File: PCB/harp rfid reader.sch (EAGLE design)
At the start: 38 parts, among them IC1 FT232RL, IC2 LP5907MFX-3.3, IC3 ATXMEGAxxxA4U-AU, Q1 BC817-40W, U1 ID-12/20SMD

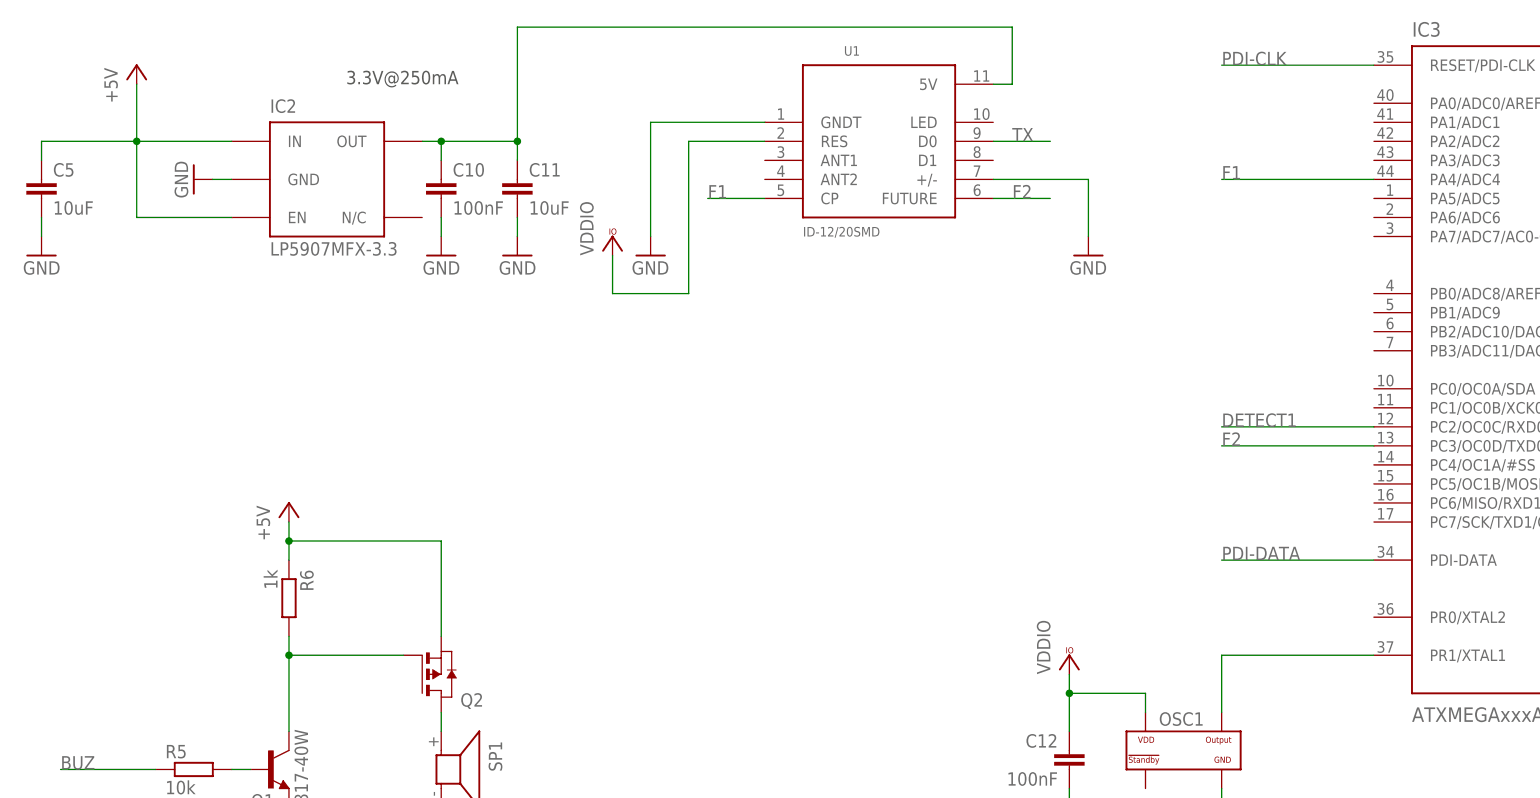
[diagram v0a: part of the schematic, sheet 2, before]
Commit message: Added 3 new capacitors.
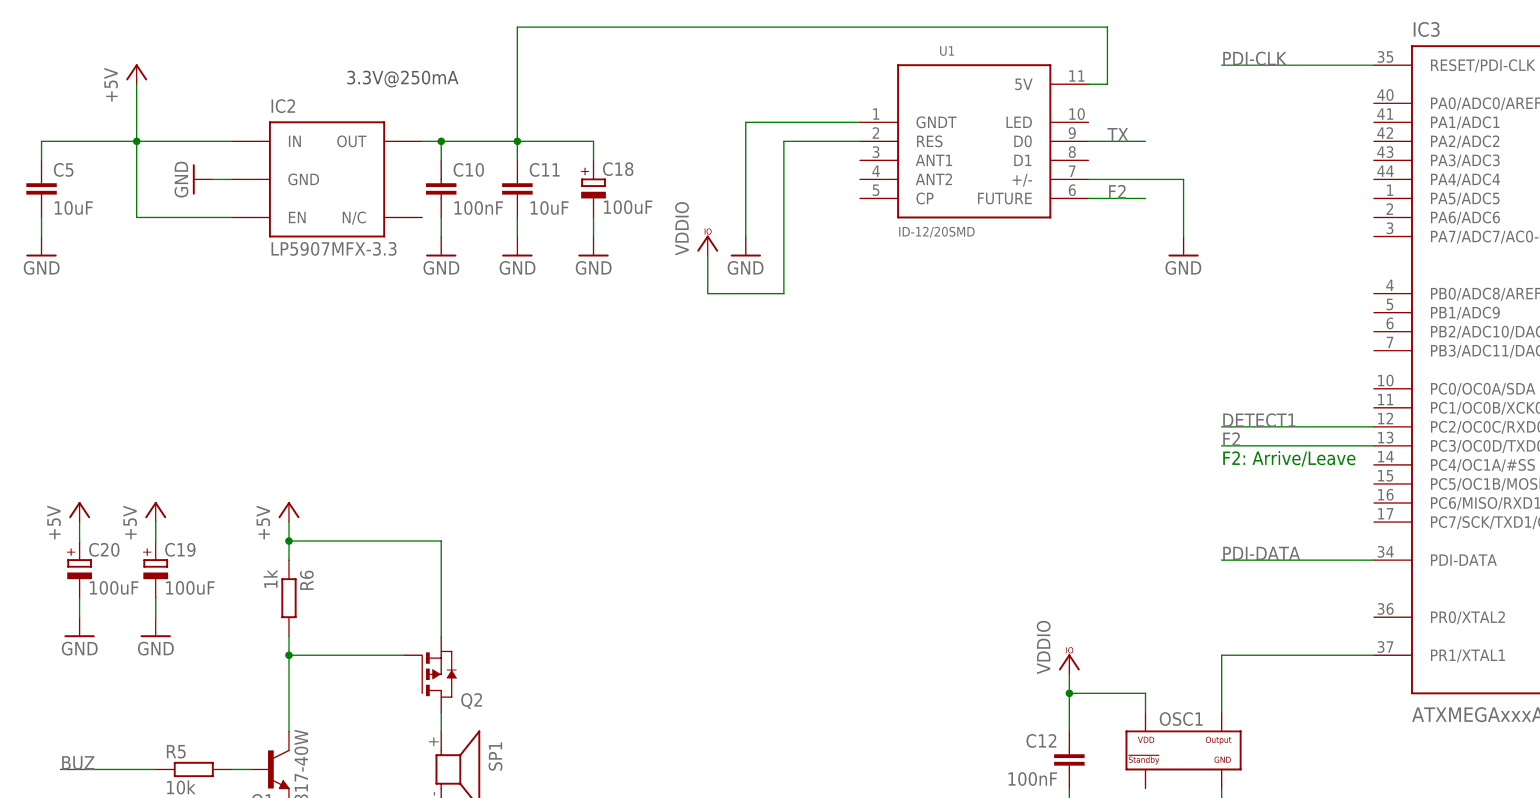
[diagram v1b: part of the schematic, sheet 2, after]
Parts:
- added C18, C19, C20: 100uF, rcl:CPOL-EUCT3216
- C7: value 4.7uF -> 10uF; device rcl:CPOL-EUA/3216-18W -> rcl:C-EUC0603
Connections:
- removed net F1: IC3.PA4/ADC4, U1.CP
- net +5V: now also C19.+, C20.+, C7.1; no longer C7.+
- net GND: now also C18.-, C19.-, C20.-, C7.2; no longer C7.-
- net N$1: now also C18.+
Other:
- note added: "F2: Arrive/Leave"
- note removed: "Case A"
- moved on the sheet: U1

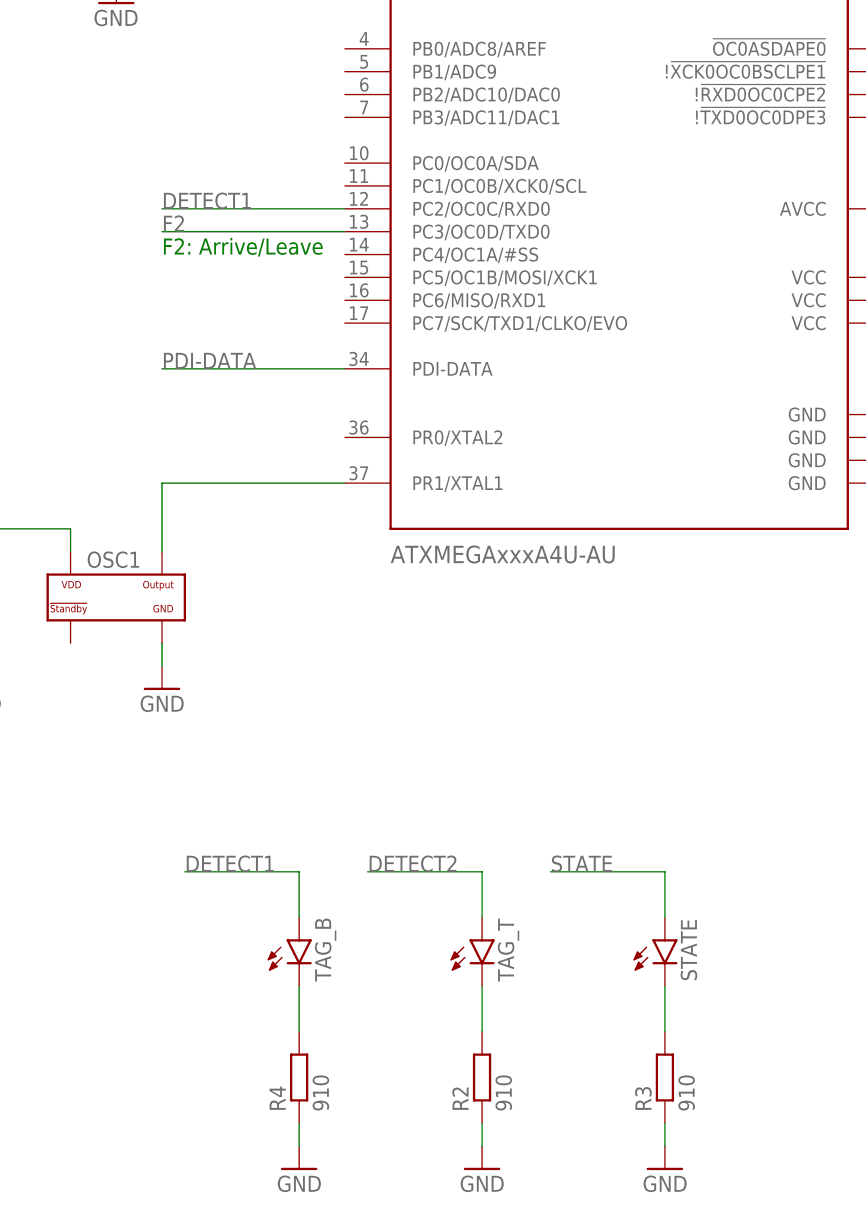
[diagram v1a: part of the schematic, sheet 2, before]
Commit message: Corrected STATE and DETECT lines and increased LED resistors.
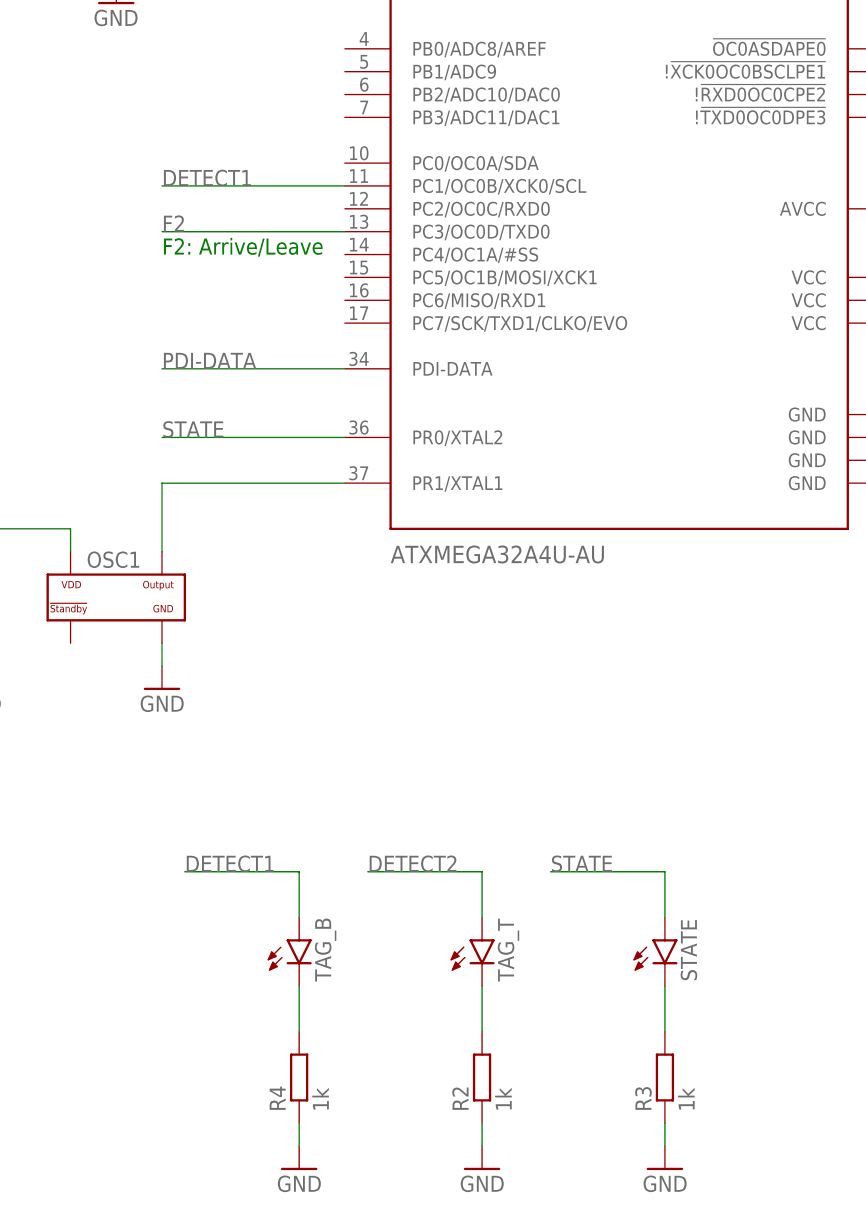
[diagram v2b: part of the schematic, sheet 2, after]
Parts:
- IC3: value ATXMEGAxxxA4U-AU -> ATXMEGA32A4U-AU
- R2, R3, R4: value 910 -> 1k
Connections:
- net DETECT1: now also IC3.PC1/OC0B/XCK0/SCL; no longer IC3.PC2/OC0C/RXD0
- net STATE: now also IC3.PR0/XTAL2
